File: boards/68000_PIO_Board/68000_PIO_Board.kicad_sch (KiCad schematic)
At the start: 20 parts, among them J1 Conn_02x08_Odd_Even, J10 Conn_01x08, J11 Conn_01x08, J12 Conn_01x08, J13 Conn_01x10, J2 Conn_02x08_Odd_Even, J3 Conn_02x08_Odd_Even, J4 Conn_01x03, J5 Conn_01x03, J6 Conn_02x04_Odd_Even, J7 Conn_02x04_Odd_Even, J8 Conn_02x04_Odd_Even, J9 Conn_02x04_Odd_Even, M1 RC2014_40_PIN, U1 68230, U2 68230, U3 74LS138

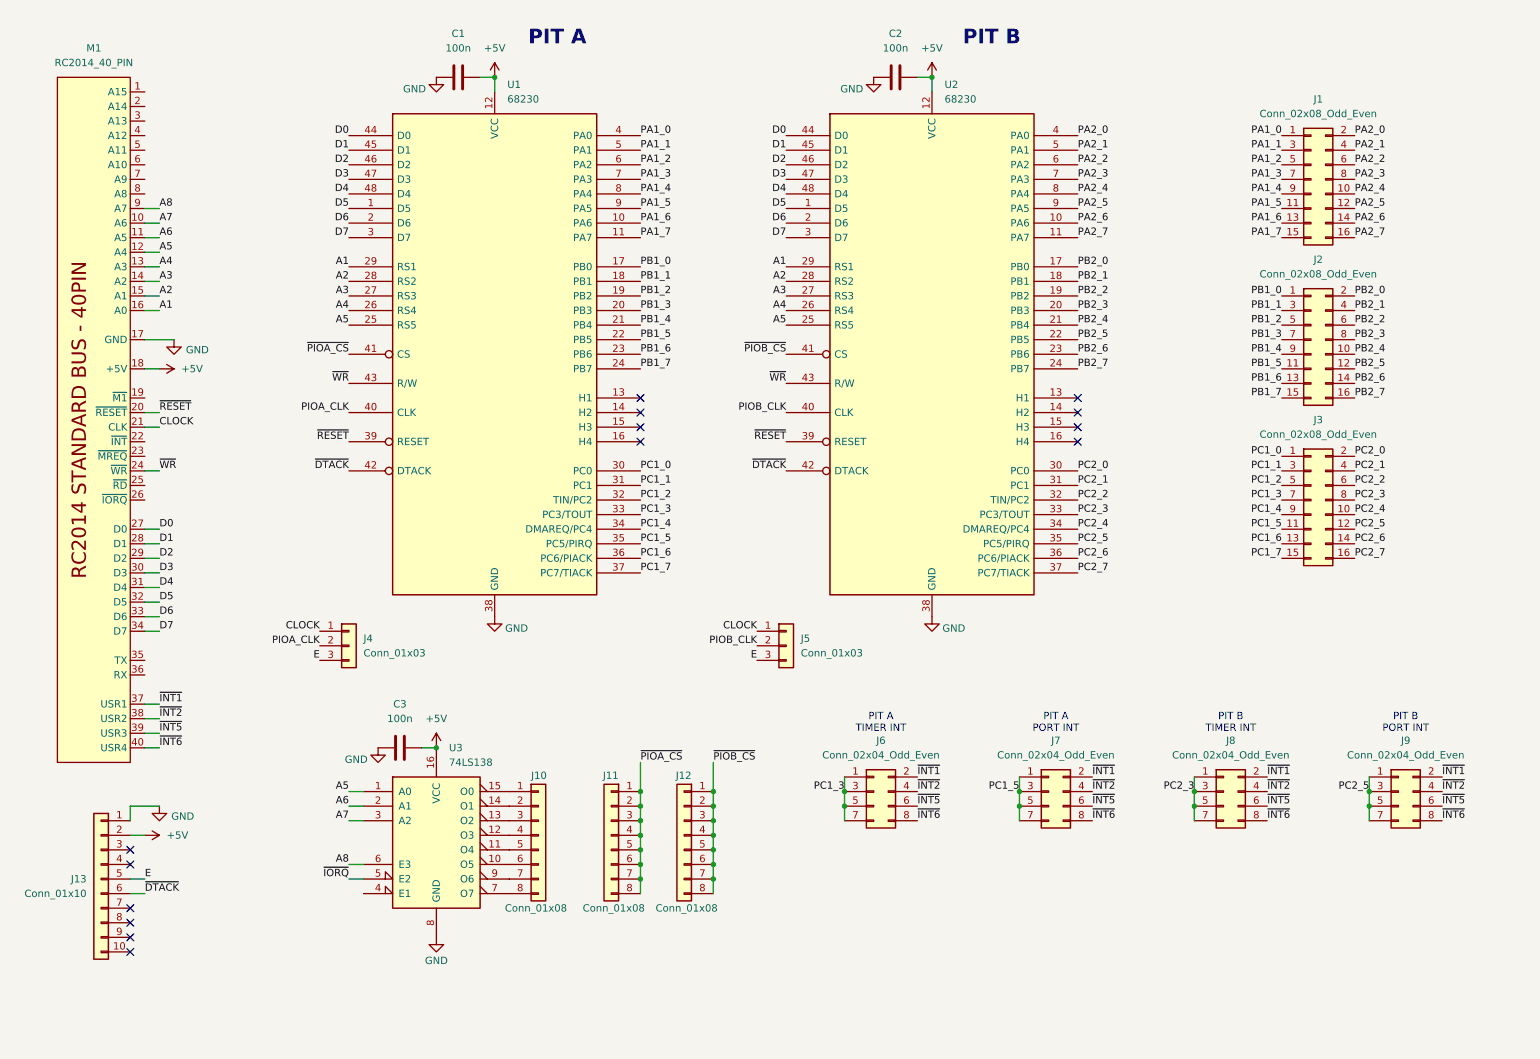
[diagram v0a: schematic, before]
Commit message: Update to v2 board set
Lots of updates to reflect the new v2 boards that use the full RCBus 80 pins as well as slight modifications to the various test programs to reflect the new IO and MEM space addresses.
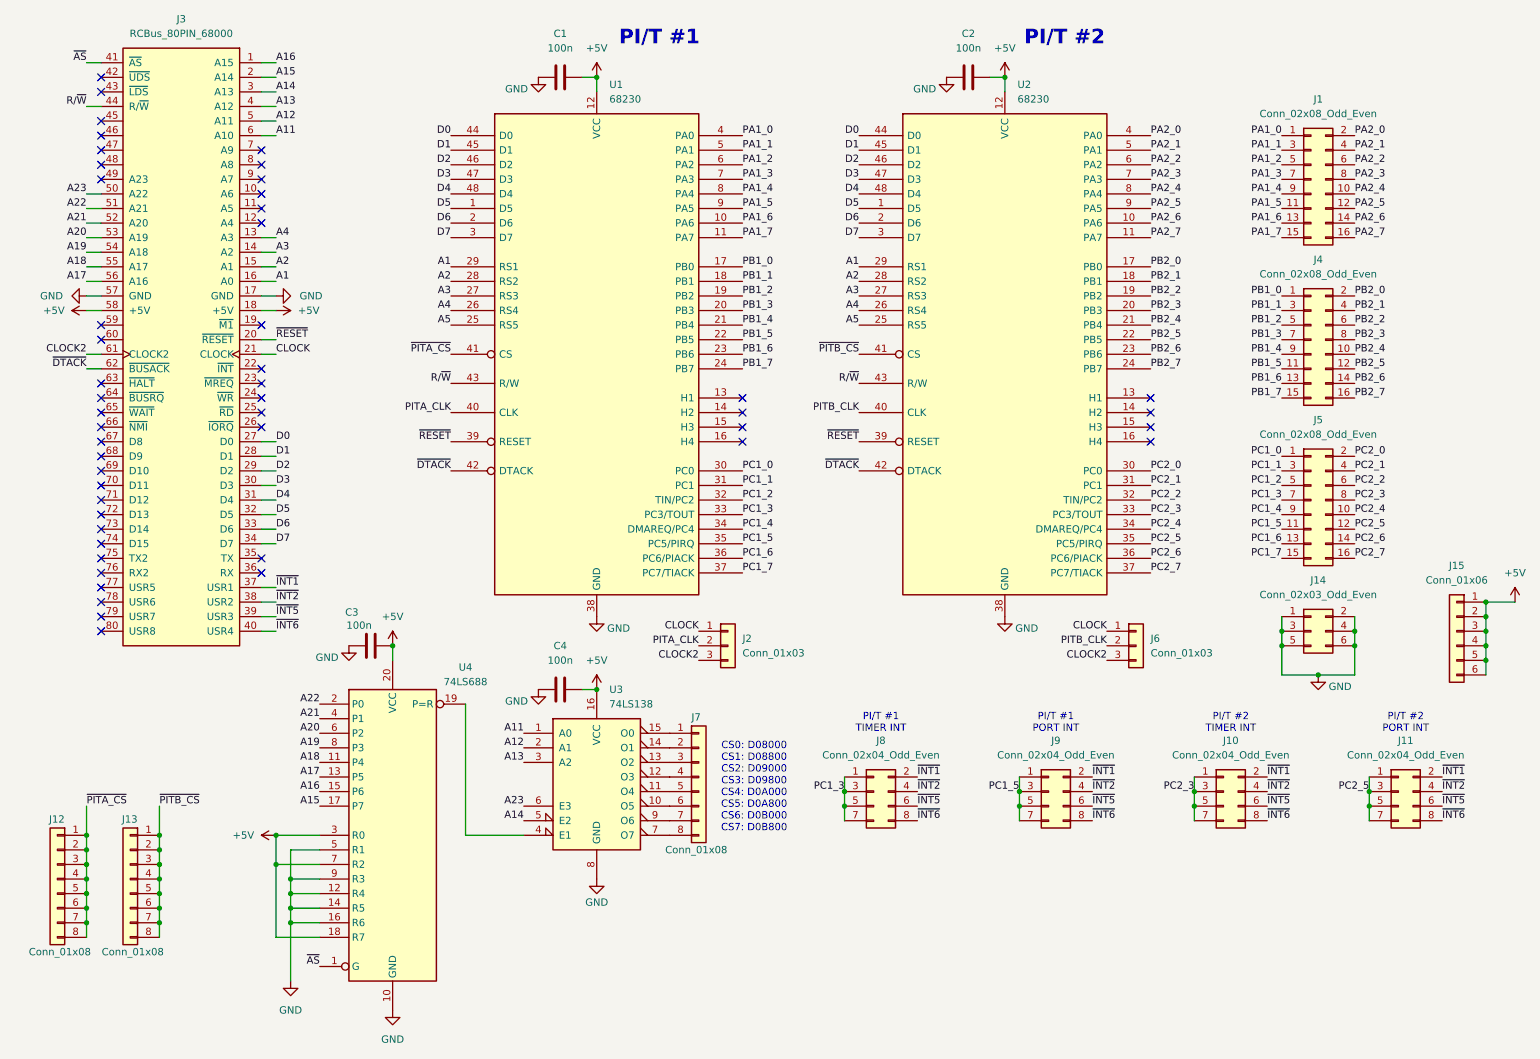
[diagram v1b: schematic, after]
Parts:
- removed J10: Conn_01x08, MyLibrary2023:PinHeader_1x08_P2.54mm_Vertical, symbol Connector_Generic:Conn_01x08
- removed J13: Conn_01x10, MyLibrary2023:PinHeader_1x10_P2.54mm_Vertical, symbol Connector_Generic:Conn_01x10
- removed M1: RC2014_40_PIN, MyLibrary2023:RC2014_STD_40_PIN, symbol MyLibrary2023:RC2014_40_PIN
- added C4: 100n, Capacitor_THT:C_Disc_D5.0mm_W2.5mm_P2.50mm, symbol Device:C
- added J14: Conn_02x03_Odd_Even, Connector_PinSocket_2.54mm:PinSocket_2x03_P2.54mm_Vertical, symbol Connector_Generic:Conn_02x03_Odd_Even
- added J15: Conn_01x06, Connector_PinSocket_2.54mm:PinSocket_1x06_P2.54mm_Vertical, symbol Connector_Generic:Conn_01x06
- added J3: RCBus_80PIN_68000, MyLibrary2023:RCBus_80p_Medium, symbol MyLibrary2023:RCBus_80PIN_68000
- added J7: Conn_01x08, Connector_PinHeader_2.54mm:PinHeader_1x08_P2.54mm_Vertical, symbol Connector_Generic:Conn_01x08
- added U4: 74LS688, MyLibrary2023:DIP-20_W7.62mm_Socket, symbol 74xx:74LS688
- renumbered J8 to J10, J9 to J11, J11 to J12, J12 to J13, J4 to J2, J2 to J4, J3 to J5, J5 to J6, J6 to J8, J7 to J9
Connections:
- net +5V: now also C4.2, J15.1 (Pin_1), J15.2 (Pin_2), J15.3 (Pin_3), J15.4 (Pin_4), J15.5 (Pin_5), J15.6 (Pin_6), J3.18 (+5V), J3.58 (+5V), U4.18 (R7), U4.20 (VCC), U4.3 (R0), U4.7 (R2)
- net A1: now also J3.16 (A0)
- net A2: now also J3.15 (A1)
- net A3: now also J3.14 (A2)
- net A4: now also J3.13 (A3)
- net A5: no longer U3.1 (A0)
- net CLOCK: now also J3.21 (CLOCK)
- net D0: now also J3.27 (D0)
- net D1: now also J3.28 (D1)
- net D2: now also J3.29 (D2)
- net D3: now also J3.30 (D3)
- net D4: now also J3.31 (D4)
- net D5: now also J3.32 (D5)
- net D6: now also J3.33 (D6)
- net D7: now also J3.34 (D7)
- net GND: now also C4.1, J14.1 (Pin_1), J14.2 (Pin_2), J14.3 (Pin_3), J14.4 (Pin_4), J14.5 (Pin_5), J14.6 (Pin_6), J3.17 (GND), J3.57 (GND), U4.10 (GND), U4.12 (R4), U4.14 (R5), U4.16 (R6), U4.5 (R1), U4.9 (R3)
- net ~{DTACK}: now also J3.62 (~{BUSACK})
- net ~{INT1}: now also J3.37 (USR1)
- net ~{INT2}: now also J3.38 (USR2)
- net ~{INT5}: now also J3.39 (USR3)
- net ~{INT6}: now also J3.40 (USR4)
- net ~{RESET}: now also J3.20 (~{RESET})
- net at U3.15 (O0): now also J7.1 (Pin_1)
- net at U3.14 (O1): now also J7.2 (Pin_2)
- net at U3.13 (O2): now also J7.3 (Pin_3)
- net at U3.12 (O3): now also J7.4 (Pin_4)
- net at U3.11 (O4): now also J7.5 (Pin_5)
- net at U3.10 (O5): now also J7.6 (Pin_6)
- net at U3.9 (O6): now also J7.7 (Pin_7)
- net at U3.7 (O7): now also J7.8 (Pin_8)
- net at U3.4 (E1): now also U4.19 (P=R)
- net A6 renamed A12
- net A12: now also J3.5 (A11)
- net A7 renamed A13
- net A13: now also J3.4 (A12)
- net A8 renamed A23
- net A23: now also J3.50 (A22)
- net E renamed CLOCK2
- net CLOCK2: now also J3.61 (CLOCK2)
- net PIOA_CLK renamed PITA_CLK
- net PIOB_CLK renamed PITB_CLK
- net ~{IORQ} renamed A14
- net A14: now also J3.3 (A13)
- net ~{PIOA_CS} renamed ~{PITA_CS}
- net ~{PIOB_CS} renamed ~{PITB_CS}
- net ~{WR} renamed R/~{W}
- net R/~{W}: now also J3.44 (R/~{W})
- new net A11: J3.6 (A10), U3.1 (A0)
- new net A15: J3.2 (A14), U4.17 (P7)
- new net A16: J3.1 (A15), U4.15 (P6)
- new net A17: J3.56 (A16), U4.13 (P5)
- new net A18: J3.55 (A17), U4.11 (P4)
- new net A19: J3.54 (A18), U4.8 (P3)
- new net A20: J3.53 (A19), U4.6 (P2)
- new net A21: J3.52 (A20), U4.4 (P1)
- new net A22: J3.51 (A21), U4.2 (P0)
- new net ~{AS}: J3.41 (~{AS}), U4.1 (G)
- no-connect marks 14 -> 49
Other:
- note added: "CS0: D08000 CS1: D08800 CS2: D09000 CS3: D09800 CS4: D0A000 CS5: D0A800 CS6: D0B000 CS7: D0B800"
- note added: "PI/T #1"
- note added: "PI/T #1 PORT INT"
- note added: "PI/T #1 TIMER INT"
- note added: "PI/T #2"
- note added: "PI/T #2 PORT INT"
- note added: "PI/T #2 TIMER INT"
- note removed: "PIT A"
- note removed: "PIT A PORT INT"
- note removed: "PIT A TIMER INT"
- note removed: "PIT B"
- note removed: "PIT B PORT INT"
- note removed: "PIT B TIMER INT"
- moved on the sheet: C1, C2, J12, J13, J2, J6, U1, U2
